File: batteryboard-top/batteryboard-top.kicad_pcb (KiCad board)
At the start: 2 copper layers, 46.8 x 46.8 mm, 7 parts, among them J1 Conn_02x05_Odd_Even, J2 Conn_02x05_Odd_Even

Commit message: move +Y solar connector to make it less symmetric
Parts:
- moved J2 8.10 mm to (150.0, 87.4)
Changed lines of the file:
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@@
   )
   (footprint "batteryboard:FTS-105-XX-YY-DV-A" (layer "F.Cu")
-    (at 150 95.5 90)
+    (at 149.9725 87.4 90)
     (descr "FTS-105-XX-YY-DV-A")
     (tags "Connector")
@@
   (gr_line (start 171.199988 80.099992) (end 173.4 80.099992) (layer "Edge.Cuts") (width 0.0254))
   (gr_arc (start 127.399999 90.099998) (mid 127.117156 89.982842) (end 127 89.699998) (layer "Edge.Cuts") (width 0.0254))
-  (gr_arc (start 173.800008 119.49999) (mid 173.682851 119.782833) (end 173.400009 119.899989) (layer "Edge.Cuts") (width 0.0254))
+  (gr_arc (start 173.800008 119.49999) (mid 173.682852 119.782833) (end 173.400009 119.899989) (layer "Edge.Cuts") (width 0.0254))
   (gr_line (start 170.799988 112.500004) (end 170.799988 80.499991) (layer "Edge.Cuts") (width 0.0254))
   (gr_line (start 130 112.499993) (end 129.999994 90.499997) (layer "Edge.Cuts") (width 0.0254))
   (gr_line (start 129.599995 90.099998) (end 127.399999 90.099998) (layer "Edge.Cuts") (width 0.0254))
   (gr_arc (start 127 73.500005) (mid 127.117155 73.217153) (end 127.399999 73.099981) (layer "Edge.Cuts") (width 0.0254))
-  (gr_arc (start 173.400009 112.900003) (mid 173.682843 113.017163) (end 173.800008 113.300002) (layer "Edge.Cuts") (width 0.0254))
+  (gr_arc (start 173.400009 112.900003) (mid 173.682845 113.017166) (end 173.800008 113.300002) (layer "Edge.Cuts") (width 0.0254))
   (gr_arc (start 129.999994 112.500004) (mid 129.882831 112.78284) (end 129.599995 112.900003) (layer "Edge.Cuts") (width 0.0254))
   (gr_arc (start 127.399999 119.899989) (mid 127.117158 119.782831) (end 127 119.49999) (layer "Edge.Cuts") (width 0.0254))
-  (gr_arc (start 170.799988 80.499991) (mid 170.917144 80.217141) (end 171.199988 80.099992) (layer "Edge.Cuts") (width 0.0254))
+  (gr_arc (start 170.799988 80.499991) (mid 170.917141 80.217144) (end 171.199988 80.099992) (layer "Edge.Cuts") (width 0.0254))
   (gr_line (start 173.800008 119.49999) (end 173.800008 113.300002) (layer "Edge.Cuts") (width 0.0254))
   (gr_line (start 173.400009 119.899989) (end 127.399999 119.899989) (layer "Edge.Cuts") (width 0.0254))
-  (gr_arc (start 173.400009 73.099981) (mid 173.68286 73.217148) (end 173.800008 73.500005) (layer "Edge.Cuts") (width 0.0254))
+  (gr_arc (start 173.400009 73.099981) (mid 173.682859 73.217147) (end 173.800008 73.500005) (layer "Edge.Cuts") (width 0.0254))
   (gr_arc (start 173.800008 79.699993) (mid 173.68285 79.982834) (end 173.400009 80.099992) (layer "Edge.Cuts") (width 0.0254))
   (gr_arc (start 127 113.300002) (mid 127.117153 113.017156) (end 127.399999 112.900003) (layer "Edge.Cuts") (width 0.0254))

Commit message: Updated connector position on top batteryboard
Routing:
- net BATT_P: track 34.9 -> 26.6 mm
- net COIL_P: track 31.8 -> 26.3 mm
- net COIL_N: track 25.9 -> 22.5 mm
- net VBUS: track 25.4 -> 22.0 mm
- net SCL3: track 25.9 -> 22.5 mm
- net SDA3: track 30.2 -> 27.2 mm
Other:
- board text added: "29-JUN-22"
- board text added: "Top Battery Board Rev 1.1 Gaurav Savant"
- board text added: "v01.1"
- board text removed: "09-JUN-22"
- board text removed: "Top Battery Board Rev 1 Gaurav Savant"
- board text removed: "v01"
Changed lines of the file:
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@@
     (pad "10" smd rect (at 2.54 -1.8425 90) (size 0.74 1.675) (layers "B.Cu" "B.Paste" "B.Mask")
       (net 2 "VBUS") (pinfunction "Pin_10") (pintype "passive"))
-    (model "C:/Users/Neil/Desktop/avionics-batteryboard/kicad-libs/3d/FLE-105-01-G-DV-A.step"
+    (model "C:/Users/Neil/Desktop/avionics-batteryboard/kicad-libs/3d/FLE-105-01-G-DV-A.step" hide
       (offset (xyz 0 0 0.1524))
       (scale (xyz 1 1 1))
@@
   (gr_arc (start 171.199988 112.900003) (mid 170.917151 112.782841) (end 170.799988 112.500004) (layer "Edge.Cuts") (width 0.0254))
   (gr_line (start 127.399999 112.900003) (end 129.6 112.899993) (layer "Edge.Cuts") (width 0.0254))
-  (gr_text "Top Battery Board Rev 1\nGaurav Savant\n" (at 132.699989 101.7 90) (layer "F.SilkS")
+  (gr_text "Top Battery Board Rev 1.1\nGaurav Savant\n" (at 132.699989 101.7 90) (layer "F.SilkS")
     (effects (font (size 1 1) (thickness 0.15)))
   )
-  (gr_text "09-JUN-22" (at 152.318797 75.512412) (layer "F.Mask")
+  (gr_text "29-JUN-22" (at 152.318796 75.512422) (layer "F.Mask")
     (effects (font (size 0.635 0.635) (thickness 0.1524)) (justify right))
   )
-  (gr_text "v01" (at 154.3 77.9) (layer "F.Mask")
+  (gr_text "v01.1" (at 154.299996 77.899997) (layer "F.Mask")
     (effects (font (size 0.635 0.635) (thickness 0.1524)) (justify right))
   )
-  (segment (start 146.16 92.96) (end 147.965 92.96) (width 0.4572) (layer "F.Cu") (net 2))
-  (segment (start 133.8 80.6) (end 146.16 92.96) (width 0.4572) (layer "F.Cu") (net 2))
   (segment (start 129.5 80.6) (end 133.8 80.6) (width 0.4572) (layer "F.Cu") (net 2))
+  (segment (start 138.06 84.86) (end 147.9375 84.86) (width 0.4572) (layer "F.Cu") (net 2))
+  (segment (start 133.8 80.6) (end 138.06 84.86) (width 0.4572) (layer "F.Cu") (net 2))
   (via (at 129.5 80.6) (size 0.8) (drill 0.4) (layers "F.Cu" "B.Cu") (free) (net 2))
   (segment (start 129.5355 80.6355) (end 129.5355 82.414) (width 0.4572) (layer "B.Cu") (net 2))
   (segment (start 129.5 80.6) (end 129.5355 80.6355) (width 0.4572) (layer "B.Cu") (net 2))
-  (via (at 152.035 96.77) (size 0.8) (drill 0.4) (layers "F.Cu" "B.Cu") (net 5))
-  (segment (start 152.035 90.435) (end 152.035 96.77) (width 0.4572) (layer "B.Cu") (net 5))
-  (segment (start 133.220495 86.155428) (end 147.755428 86.155428) (width 0.4572) (layer "B.Cu") (net 5))
-  (segment (start 147.755428 86.155428) (end 152.035 90.435) (width 0.4572) (layer "B.Cu") (net 5))
-  (segment (start 154.2 95.5) (end 152.035 95.5) (width 0.254) (layer "F.Cu") (net 6))
-  (via (at 154.2 95.5) (size 0.8) (drill 0.4) (layers "F.Cu" "B.Cu") (net 6))
-  (segment (start 154.2 95.5) (end 154.2 91) (width 0.254) (layer "B.Cu") (net 6))
+  (segment (start 155.4 88.7) (end 155.37 88.67) (width 0.4572) (layer "F.Cu") (net 5))
+  (segment (start 155.37 88.67) (end 152.0075 88.67) (width 0.4572) (layer "F.Cu") (net 5))
+  (via (at 155.4 88.7) (size 0.8) (drill 0.4) (layers "F.Cu" "B.Cu") (net 5))
+  (segment (start 155.4 88.7) (end 153.9 87.2) (width 0.4572) (layer "B.Cu") (net 5))
+  (segment (start 147.755428 86.155428) (end 133.220495 86.155428) (width 0.4572) (layer "B.Cu") (net 5))
+  (segment (start 153.9 87.2) (end 148.8 87.2) (width 0.4572) (layer "B.Cu") (net 5))
+  (segment (start 148.8 87.2) (end 147.755428 86.155428) (width 0.4572) (layer "B.Cu") (net 5))
+  (segment (start 155.4 87.4) (end 152.0075 87.4) (width 0.254) (layer "F.Cu") (net 6))
+  (via (at 155.4 87.4) (size 0.8) (drill 0.4) (layers "F.Cu" "B.Cu") (net 6))
+  (segment (start 152.2 84.2) (end 148.770856 84.2) (width 0.254) (layer "B.Cu") (net 6))
   (segment (start 148.085428 84.885428) (end 133.220495 84.885428) (width 0.254) (layer "B.Cu") (net 6))
-  (segment (start 154.2 91) (end 148.085428 84.885428) (width 0.254) (layer "B.Cu") (net 6))
-  (segment (start 135.154 84.954) (end 145.7 95.5) (width 0.254) (layer "F.Cu") (net 7))
-  (segment (start 145.7 95.5) (end 147.965 95.5) (width 0.254) (layer "F.Cu") (net 7))
+  (segment (start 148.770856 84.2) (end 148.085428 84.885428) (width 0.254) (layer "B.Cu") (net 6))
+  (segment (start 155.4 87.4) (end 152.2 84.2) (width 0.254) (layer "B.Cu") (net 6))
   (segment (start 128 84.954) (end 135.154 84.954) (width 0.254) (layer "F.Cu") (net 7))
+  (segment (start 135.154 84.954) (end 137.6 87.4) (width 0.254) (layer "F.Cu") (net 7))
+  (segment (start 137.6 87.4) (end 147.9375 87.4) (width 0.254) (layer "F.Cu") (net 7))
   (via (at 128 84.954) (size 0.8) (drill 0.4) (layers "F.Cu" "B.Cu") (free) (net 7))
   (segment (start 128 84.954) (end 129.466923 84.954) (width 0.254) (layer "B.Cu") (net 7))
   (segment (start 129.466923 84.954) (end 129.535495 84.885428) (width 0.254) (layer "B.Cu") (net 7))
-  (segment (start 155.57 94.23) (end 152.136998 94.23) (width 0.4572) (layer "F.Cu") (net 8))
-  (segment (start 155.6 94.2) (end 155.57 94.23) (width 0.4572) (layer "F.Cu") (net 8))
-  (via (at 155.6 94.2) (size 0.8) (drill 0.4) (layers "F.Cu" "B.Cu") (net 8))
-  (segment (start 155.6 94.2) (end 155.6 90.6) (width 0.4572) (layer "B.Cu") (net 8))
-  (segment (start 148.684 83.684) (end 133.7885 83.684) (width 0.4572) (layer "B.Cu") (net 8))
-  (segment (start 155.6 90.6) (end 148.684 83.684) (width 0.4572) (layer "B.Cu") (net 8))
+  (segment (start 155.4 86.1) (end 155.37 86.13) (width 0.4572) (layer "F.Cu") (net 8))
+  (segment (start 155.37 86.13) (end 152.0075 86.13) (width 0.4572) (layer "F.Cu") (net 8))
+  (via (at 155.4 86.1) (size 0.8) (drill 0.4) (layers "F.Cu" "B.Cu") (net 8))
+  (segment (start 152.6 83.3) (end 148.1 83.3) (width 0.4572) (layer "B.Cu") (net 8))
+  (segment (start 147.716 83.684) (end 133.7885 83.684) (width 0.4572) (layer "B.Cu") (net 8))
+  (segment (start 148.1 83.3) (end 147.716 83.684) (width 0.4572) (layer "B.Cu") (net 8))
+  (segment (start 155.4 86.1) (end 152.6 83.3) (width 0.4572) (layer "B.Cu") (net 8))
   (segment (start 128 83.6) (end 128.4 84) (width 0.4572) (layer "F.Cu") (net 9))
-  (segment (start 135.5 84) (end 145.73 94.23) (width 0.4572) (layer "F.Cu") (net 9))
+  (segment (start 137.63 86.13) (end 147.9375 86.13) (width 0.4572) (layer "F.Cu") (net 9))
+  (segment (start 135.5 84) (end 137.63 86.13) (width 0.4572) (layer "F.Cu") (net 9))
   (segment (start 128.4 84) (end 135.5 84) (width 0.4572) (layer "F.Cu") (net 9))
-  (segment (start 145.73 94.23) (end 147.965 94.23) (width 0.4572) (layer "F.Cu") (net 9))
   (via (at 128 83.6) (size 0.8) (drill 0.4) (layers "F.Cu" "B.Cu") (net 9))
   (segment (start 129.535495 83.615428) (end 128.015428 83.615428) (width 0.4572) (layer "B.Cu") (net 9))
   (segment (start 128.015428 83.615428) (end 128 83.6) (width 0.4572) (layer "B.Cu") (net 9))
-  (segment (start 157.06 92.96) (end 152.136998 92.96) (width 0.4572) (layer "F.Cu") (net 10))
-  (segment (start 157.1 93) (end 157.06 92.96) (width 0.4572) (layer "F.Cu") (net 10))
-  (via (at 157.1 93) (size 0.8) (drill 0.4) (layers "F.Cu" "B.Cu") (net 10))
-  (segment (start 157.1 93) (end 157.1 90.2) (width 0.4572) (layer "B.Cu") (net 10))
-  (segment (start 149.245428 82.345428) (end 133.220495 82.345428) (width 0.4572) (layer "B.Cu") (net 10))
-  (segment (start 157.1 90.2) (end 149.245428 82.345428) (width 0.4572) (layer "B.Cu") (net 10))
+  (segment (start 155.39 84.86) (end 152.0075 84.86) (width 0.4572) (layer "F.Cu") (net 10))
+  (segment (start 155.4 84.85) (end 155.39 84.86) (width 0.4572) (layer "F.Cu") (net 10))
+  (via (at 155.4 84.85) (size 0.8) (drill 0.4) (layers "F.Cu" "B.Cu") (net 10))
+  (segment (start 155.4 84.85) (end 152.895428 82.345428) (width 0.4572) (layer "B.Cu") (net 10))
+  (segment (start 152.895428 82.345428) (end 133.220495 82.345428) (width 0.4572) (layer "B.Cu") (net 10))
   (zone (net 1) (net_name "GND") (layers F&B.Cu) (hatch edge 0.508)
     (connect_pads yes (clearance 0.381))

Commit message: Recheck boards and re-export models
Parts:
- J1: value Conn_02x05_Odd_Even -> FLE-105-01-G-DV-A
- J2: value Conn_02x05_Odd_Even -> FLE-105-01-G-DV-A; footprint batteryboard:FTS-105-XX-YY-DV-A -> batteryboard:SAMTEC_FLE-105-01-G-DV-A
- moved J2 10.2 mm to (160.1, 87.4)
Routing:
- net SCL3: track 22.5 -> 46.1 mm
- net COIL_N: track 22.5 -> 45.3 mm
- net VBUS: track 22.0 -> 35.4 mm
- net SDA3: track 27.2 -> 26.1 mm
- net +3V3: track 26.6 -> 26.1 mm
- net BATT_P: track 26.6 -> 26.1 mm
- net GND: track 0.00 -> 0.04 mm, vias 0 -> 2

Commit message: Added +Y rail outline to top board silkscreen
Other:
- board text removed: "Top Battery Board Rev 1.1 Gaurav Savant"
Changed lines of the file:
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@@
     )
   )
+  (gr_line (start 166.799997 112.900003) (end 134.000011 112.900003) (layer "F.SilkS") (width 0.127))
+  (gr_circle (center 170.3 116.4) (end 170.3 114.65) (layer "F.SilkS") (width 0.0254) (fill none))
+  (gr_circle (center 170.3 76.6) (end 170.3 74.85) (layer "F.SilkS") (width 0.0254) (fill none))
+  (gr_circle (center 130.5 116.4) (end 130.5 114.65) (layer "F.SilkS") (width 0.0254) (fill none))
+  (gr_circle (center 170.3 116.4) (end 170.3 114.65) (layer "F.SilkS") (width 0.0254) (fill none))
+  (gr_circle (center 130.5 116.4) (end 130.5 114.65) (layer "F.SilkS") (width 0.0254) (fill none))
+  (gr_circle (center 158.800013 116.399996) (end 160.550013 116.399996) (layer "F.SilkS") (width 0.127) (fill none))
+  (gr_circle (center 141.999995 76.599999) (end 143.749995 76.599999) (layer "F.SilkS") (width 0.127) (fill none))
+  (gr_line (start 166.799997 80.099992) (end 166.799997 112.900003) (layer "F.SilkS") (width 0.127))
+  (gr_circle (center 170.3 76.6) (end 170.3 74.85) (layer "F.SilkS") (width 0.0254) (fill none))
+  (gr_circle (center 170.3 76.6) (end 170.3 74.85) (layer "F.SilkS") (width 0.0254) (fill none))
+  (gr_circle (center 130.5 76.6) (end 130.5 74.85) (layer "F.SilkS") (width 0.0254) (fill none))
+  (gr_circle (center 130.5 76.6) (end 130.5 74.85) (layer "F.SilkS") (width 0.0254) (fill none))
+  (gr_circle (center 170.3 116.4) (end 170.3 114.65) (layer "F.SilkS") (width 0.0254) (fill none))
+  (gr_circle (center 137.000005 116.399996) (end 138.750005 116.399996) (layer "F.SilkS") (width 0.127) (fill none))
+  (gr_line (start 134.000011 80.099992) (end 166.799997 80.099992) (layer "F.SilkS") (width 0.127))
+  (gr_circle (center 130.5 116.4) (end 130.5 114.65) (layer "F.SilkS") (width 0.0254) (fill none))
+  (gr_circle (center 170.3 116.4) (end 170.3 114.65) (layer "F.SilkS") (width 0.0254) (fill none))
+  (gr_circle (center 130.5 76.6) (end 130.5 74.85) (layer "F.SilkS") (width 0.0254) (fill none))
+  (gr_circle (center 130.5 76.6) (end 130.5 74.85) (layer "F.SilkS") (width 0.0254) (fill none))
+  (gr_circle (center 163.800003 76.599999) (end 165.550003 76.599999) (layer "F.SilkS") (width 0.127) (fill none))
+  (gr_circle (center 130.5 116.4) (end 130.5 114.65) (layer "F.SilkS") (width 0.0254) (fill none))
+  (gr_line (start 134.000011 112.900003) (end 134.000011 80.099992) (layer "F.SilkS") (width 0.127))
   (gr_line (start 127 89.699998) (end 127 73.500005) (layer "Edge.Cuts") (width 0.0254))
   (gr_line (start 171.199988 80.099992) (end 173.4 80.099992) (layer "Edge.Cuts") (width 0.0254))
@@
   (gr_arc (start 171.199988 112.900003) (mid 170.917151 112.782841) (end 170.799988 112.500004) (layer "Edge.Cuts") (width 0.0254))
   (gr_line (start 127.399999 112.900003) (end 129.6 112.899993) (layer "Edge.Cuts") (width 0.0254))
-  (gr_text "Top Battery Board Rev 1.1\nGaurav Savant\n" (at 132.699989 101.7 90) (layer "F.SilkS")
-    (effects (font (size 1 1) (thickness 0.15)))
-  )
   (gr_text "29-JUN-22" (at 152.318796 75.512422) (layer "F.Mask")
     (effects (font (size 0.635 0.635) (thickness 0.1524)) (justify right))

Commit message: modified/standardized silkscreen
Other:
- board text added: "Top Battery Board"
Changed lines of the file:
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@@
   (gr_arc (start 171.199988 112.900003) (mid 170.917151 112.782841) (end 170.799988 112.500004) (layer "Edge.Cuts") (width 0.0254))
   (gr_line (start 127.399999 112.900003) (end 129.6 112.899993) (layer "Edge.Cuts") (width 0.0254))
+  (gr_text "Top Battery Board" (at 131.6 103.6 90) (layer "F.SilkS")
+    (effects (font (size 1.2 1.2) (thickness 0.2)))
+  )
   (gr_text "29-JUN-22" (at 152.318796 75.512422) (layer "F.Mask")
     (effects (font (size 0.635 0.635) (thickness 0.1524)) (justify right))

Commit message: Export New Gerbers
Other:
- board text added: "06-JUL-22"
- board text removed: "29-JUN-22"
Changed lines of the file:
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@@
       (drillshape 0)
       (scaleselection 1)
-      (outputdirectory "../gerbers/batteryboard-top (06-13-22)/")
+      (outputdirectory "../gerbers/batteryboard-top (07-06-22)/")
     )
   )
@@
   (gr_arc (start 171.199988 112.900003) (mid 170.917151 112.782841) (end 170.799988 112.500004) (layer "Edge.Cuts") (width 0.0254))
   (gr_line (start 127.399999 112.900003) (end 129.6 112.899993) (layer "Edge.Cuts") (width 0.0254))
-  (gr_text "Top Battery Board" (at 131.6 103.6 90) (layer "F.SilkS")
-    (effects (font (size 1.2 1.2) (thickness 0.2)))
+  (gr_text "Top Battery Board" (at 131.850003 101.124995 90) (layer "F.SilkS")
+    (effects (font (size 0.889 0.889) (thickness 0.127)))
   )
-  (gr_text "29-JUN-22" (at 152.318796 75.512422) (layer "F.Mask")
+  (gr_text "06-JUL-22" (at 152.318796 75.512422) (layer "F.Mask")
     (effects (font (size 0.635 0.635) (thickness 0.1524)) (justify right))
   )

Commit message: B1/03 updates
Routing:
- net BATT_P: track 26.1 -> 34.7 mm, vias 1 -> 3
- net GND: track 0.04 -> 0.00 mm, vias 2 -> 3
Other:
- board text added: "06-SEP-22"
- board text added: "Rev B1/03"
- board text removed: "06-JUL-22"
- board text removed: "v01.1"

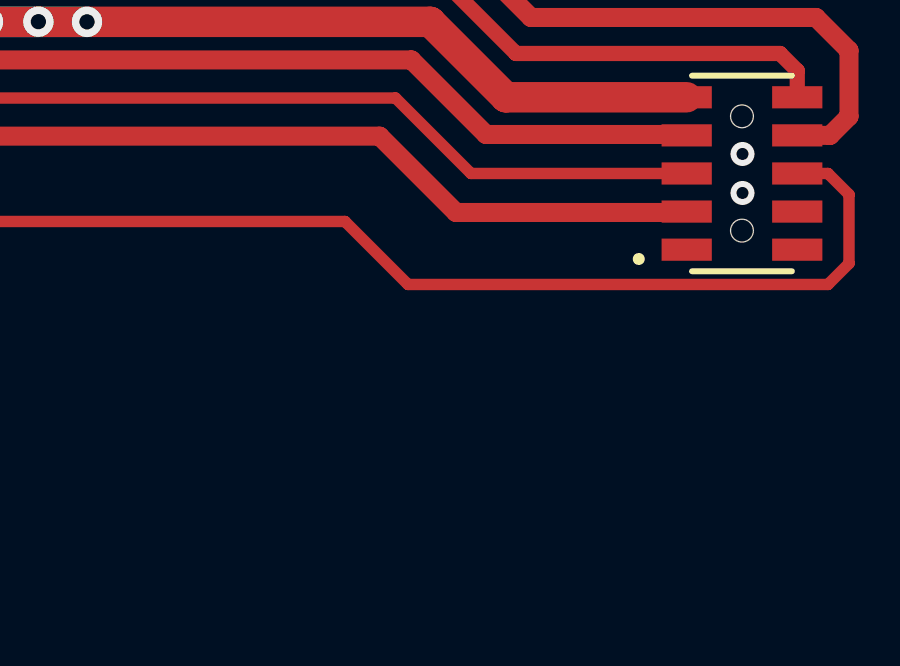
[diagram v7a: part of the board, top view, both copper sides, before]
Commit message: Added credits to top batteryboard
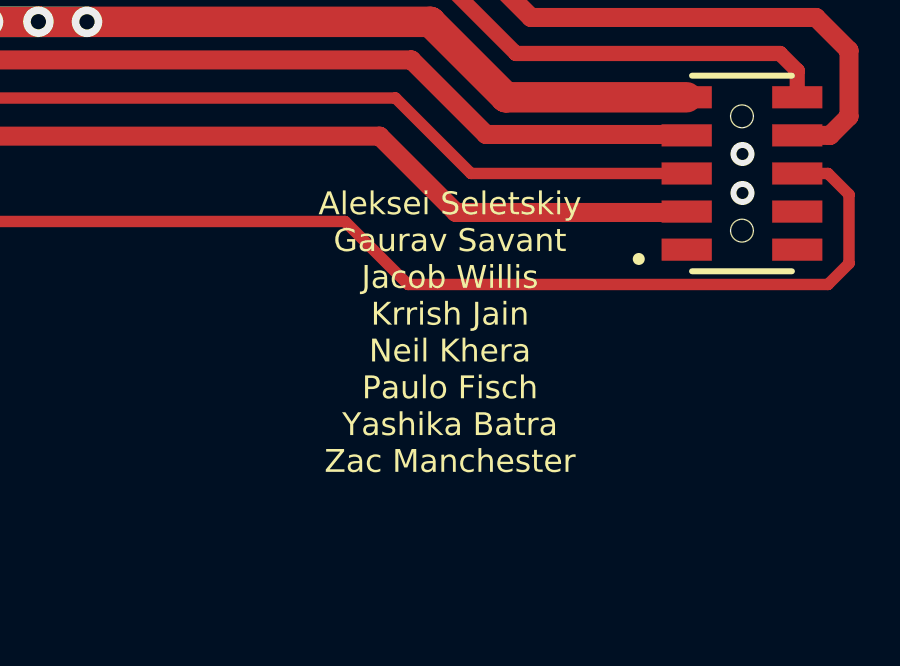
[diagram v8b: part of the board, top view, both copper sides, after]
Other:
- board text added: "Aleksei Seletskiy Gaurav Savant Jacob Willis Krrish Jain Neil Khera Paulo Fisch Yashika Batra Zac Manchester"
- board text added: "BAD?"
- board text added: "In memory of James P. Teza"
